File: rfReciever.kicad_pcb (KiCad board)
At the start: 2 copper layers, 82 x 40 mm, 27 parts, among them P1 USB_C_Plug_USB2.0, SW1 SW_Push, SW2 SW_Push, U1 XBee_SMT, U2 CP2102N-Axx-xQFN20, U3 USBLC6-2SC6

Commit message: Final Schematic preliminary pcb layout(pre-routing)
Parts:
- removed D3: LED, LED_SMD:LED_0603_1608Metric_Pad1.05x0.95mm_HandSolder
- removed D4: LED, LED_SMD:LED_0201_0603Metric
- removed P1: USB_C_Plug_USB2.0, Connector_USB:USB_C_Plug_JAE_DX07P024AJ1
- removed R10, R9: 10k, Resistor_SMD:R_0603_1608Metric_Pad0.98x0.95mm_HandSolder
- removed R8: 330, Resistor_SMD:R_0603_1608Metric_Pad0.98x0.95mm_HandSolder
- removed SW2: SW_Push, Button_Switch_THT:SW_PUSH_6mm_H4.3mm
- removed U2: CP2102N-Axx-xQFN20, Audio_Module:QFN24_CP2102N_SIL
- removed U3: USBLC6-2SC6, Package_TO_SOT_SMD:SOT-23-6
- added C8: 1u, Capacitor_SMD:C_0805_2012Metric, F.Cu at (93.6, 82.2)
- added D7: LED, LED_SMD:LED_0805_2012Metric, F.Cu at (77.6, 83.9)
- added D8: LED, LED_SMD:LED_0805_2012Metric, F.Cu at (122.0, 62.0)
- added D9: LED, LED_SMD:LED_0805_2012Metric, F.Cu at (118.5, 61.9)
- added P2: USB_C_Plug_USB2.0, Connector_USB:USB_C_Plug_JAE_DX07P024AJ1, F.Cu at (123.4, 71.8)
- added R11: 10K, Resistor_SMD:R_0805_2012Metric, F.Cu at (98.1, 76.9)
- added R12: 10k, Resistor_SMD:R_0805_2012Metric, F.Cu at (97.1, 83.9)
- added R15: 1K, Resistor_SMD:R_0805_2012Metric, F.Cu at (83.1, 85.9)
- added R16: 1K, Resistor_SMD:R_0805_2012Metric, F.Cu at (88.5, 61.0)
- added R17: 10k, Resistor_SMD:R_0805_2012Metric, F.Cu at (97.1, 80.9)
- added R18: 1K, Resistor_SMD:R_0805_2012Metric, F.Cu at (84.5, 61.0)
- added U4: USBLC6-2SC6, Package_TO_SOT_SMD:SOT-23-6, F.Cu at (116.0, 72.1)
- added X1: DigiXBeeRX900Micro, rfReciever-Footprints:XBeeXR900RFMicro, F.Cu at (85.1, 70.4)
- C1, C3: footprint Capacitor_SMD:C_0603_1608Metric_Pad1.08x0.95mm_HandSolder -> Capacitor_SMD:C_0805_2012Metric
- C2: footprint Capacitor_SMD:C_01005_0402Metric_Pad0.57x0.30mm_HandSolder -> Capacitor_SMD:C_0805_2012Metric
- C4: footprint Capacitor_SMD:C_0402_1005Metric_Pad0.74x0.62mm_HandSolder -> Capacitor_SMD:C_0805_2012Metric
- C5: value 1uF -> 47pF; footprint Capacitor_SMD:C_0603_1608Metric_Pad1.08x0.95mm_HandSolder -> Capacitor_SMD:C_0805_2012Metric
- C6: value 47pF -> 1uF; footprint Capacitor_SMD:C_0402_1005Metric_Pad0.74x0.62mm_HandSolder -> Capacitor_SMD:C_0805_2012Metric
- C7: footprint Capacitor_SMD:C_0805_2012Metric_Pad1.18x1.45mm_HandSolder -> Capacitor_SMD:C_0805_2012Metric
- D1: footprint LED_SMD:LED_0201_0603Metric -> LED_SMD:LED_0805_2012Metric
- D2: footprint LED_SMD:LED_0603_1608Metric_Pad1.05x0.95mm_HandSolder -> LED_SMD:LED_0805_2012Metric
- R1, R2, R3, R4: footprint Resistor_SMD:R_0603_1608Metric_Pad0.98x0.95mm_HandSolder -> Resistor_SMD:R_0805_2012Metric
- R5: value 330 -> 1K; footprint Resistor_SMD:R_0603_1608Metric_Pad0.98x0.95mm_HandSolder -> Resistor_SMD:R_0805_2012Metric
- R6: value 220 -> 1K; footprint Resistor_SMD:R_0603_1608Metric_Pad0.98x0.95mm_HandSolder -> Resistor_SMD:R_0805_2012Metric
- R7: value 220 -> 1k; footprint Resistor_SMD:R_0603_1608Metric_Pad0.98x0.95mm_HandSolder -> Resistor_SMD:R_0805_2012Metric
- SW1: value SW_Push -> RF_RESET; footprint Button_Switch_THT:SW_PUSH_6mm_H4.3mm -> Button_Switch_SMD:SW_SPST_CK_KMS2xxGP
- U1: value XBee_SMT -> CP2102N-Axx-xQFN20; footprint RF_Module:Digi_XBee_SMT -> rfReciever-Footprints:QFN50P500X500X80-29N
- moved C7 38.6 mm to (77.6, 80.6), turned to 180 degrees
- moved C6 36.9 mm to (81.1, 82.6), turned to -90 degrees
- moved SW1 30.4 mm to (89.1, 82.2)
- moved C1 30.2 mm to (104.8, 77.6)
- moved R5 29.5 mm to (112.0, 65.9), turned to 90 degrees
- moved U1 27.7 mm to (105.9, 72.6), turned to 0 degrees
- moved R7 27.7 mm to (95.1, 86.4)
- moved R1 26.0 mm to (106.0, 64.9)
- moved C2 24.8 mm to (100.6, 71.9), turned to 90 degrees
- moved R4 24.5 mm to (111.1, 77.7), turned to 180 degrees
- moved C5 23.9 mm to (84.1, 82.6), turned to -90 degrees
- moved C4 19.9 mm to (101.8, 68.1), turned to 0 degrees
- moved D1 18.7 mm to (112.0, 61.9), turned to -90 degrees
- moved C3 17.1 mm to (101.8, 65.1), turned to 0 degrees
- moved R6 9.47 mm to (115.0, 66.0), turned to 90 degrees
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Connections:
- net Net-(D1-A) renamed /BRIDGE_D1
- net Net-(D2-A) renamed /BRIDGE_D2
- C1 pad 1: /5V(in) -> +5V
- C2 pad 1: /5V(in) -> +5V
- C3 pad 2: /3.3V (out) -> +3.3V
- C4 pad 2: /3.3V (out) -> +3.3V
- C5 pad 1: /3.3V (out) -> +3.3V
- C6 pad 1: /3.3V (out) -> +3.3V
- C7 pad 1: /3.3V (out) -> +3.3V
- R1 pad 1: /3.3V (out) -> /BRIDGE_3.3
- R1 pad 2: Net-(U2-~{RST}) -> +3.3V
- R2 pad 1: Net-(U2-VBUS) -> /BRIDGE_VBUS
- R3 pad 1: /5V(in) -> +5V
- R3 pad 2: Net-(U2-VBUS) -> /BRIDGE_VBUS
- R5 pad 1: Net-(U1-DIO5/ASSOCIATE) -> /TXD(Bridge)
- R6 pad 1: Net-(U1-DIO13/UART_TX) -> /RXD(Bridge)
- R7 pad 1: Net-(U1-DIO14/UART_RX/~{CONFIG}) -> /RF_RESET
- R7 pad 2: Net-(D3-A) -> /RF_RESET
- SW1 pad 1: GND -> /RF_RESET
- SW1 pad 2: Net-(U1-RESET/OD_OUT) -> GND
- U1 pad 1: GND -> unconnected-(U1-RS485/GPIO.1-Pad1)
- U1 pad 10: Net-(U1-DIO8/SLEEP_REQUEST) -> unconnected-(U1-NC-Pad10)
- U1 pad 11: GND -> unconnected-(U1-~{SUSPEND}-Pad11)
- U1 pad 12: unconnected-(U1-DIO19/SPI_~{ATTN}-Pad12) -> GND
- U1 pad 13: GND -> unconnected-(U1-~{WAKEUP}-Pad13)
- U1 pad 15: unconnected-(U1-DIO17/SPI_~{SSEL}-Pad15) -> /CTS(Bridge)
- U1 pad 16: unconnected-(U1-DIO16/SPI_MOSI-Pad16) -> /RTS(Bridge)
- U1 pad 17: unconnected-(U1-DIO15/SPI_MISO-Pad17) -> /RXD(Bridge)
- U1 pad 18: unconnected-(U1-NC-Pad18) -> /TXD(Bridge)
- U1 pad 2: /3.3V (out) -> unconnected-(U1-CLK/GPIO.0-Pad2)
- U1 pad 21: unconnected-(U1-NC-Pad21) -> GND
- U1 pad 22: GND -> (no net)
- U1 pad 23: unconnected-(U1-NC-Pad23) -> (no net)
- U1 pad 24: unconnected-(U1-DIO4-Pad24) -> (no net)
- U1 pad 25: Net-(U1-DIO7/~{CTS}) -> (no net)
- U1 pad 26: unconnected-(U1-DIO9/ON/~{SLEEP}-Pad26) -> (no net)
- U1 pad 27: unconnected-(U1-VREF-Pad27) -> (no net)
- U1 pad 28: Net-(U1-DIO5/ASSOCIATE) -> (no net)
- U1 pad 29: Net-(U1-DIO6/~{RTS}) -> (no net)
- U1 pad 3: Net-(U1-DIO13/UART_TX) -> GND
- U1 pad 4: Net-(U1-DIO14/UART_RX/~{CONFIG}) -> /USB_D+
- U1 pad 5: unconnected-(U1-DIO12-Pad5) -> /USB_D-
- U1 pad 6: Net-(U1-RESET/OD_OUT) -> +3.3V
- U1 pad 7: Net-(U1-DIO10/RSSI/PWM0) -> +5V
- U1 pad 8: unconnected-(U1-DIO11/PWM1-Pad8) -> /BRIDGE_VBUS
- U1 pad 9: unconnected-(U1-NC-Pad9) -> /BRIDGE_3.3
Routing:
- net /3.3V (out): track 87.0 -> 0.00 mm, vias 2 -> 0
- net Net-(U1-DIO13/UART_TX): track 74.9 -> 0.00 mm, vias 4 -> 0
- net /5V(in): track 67.7 -> 0.00 mm, vias 2 -> 0
- net Net-(U1-DIO14/UART_RX/~{CONFIG}): track 66.0 -> 0.00 mm, vias 2 -> 0
- net Net-(U1-RESET/OD_OUT): track 55.3 -> 0.00 mm
- net Net-(U1-DIO6/~{RTS}): track 48.0 -> 0.00 mm, vias 2 -> 0
- net Net-(U1-DIO7/~{CTS}): track 47.5 -> 0.00 mm
- net GND: track 42.2 -> 0.00 mm, vias 23 -> 0
- net Net-(U1-DIO8/SLEEP_REQUEST): track 25.0 -> 0.00 mm
- net Net-(D4-A): track 22.7 -> 0.00 mm
- net Net-(U2-D-): track 21.2 -> 0.00 mm, vias 2 -> 0
- net /D-: track 13.0 -> 0.00 mm
- net /D+: track 11.6 -> 0.00 mm
- net /BRIDGE_D1: track 11.3 -> 0.00 mm
- net Net-(U2-~{RST}): track 10.3 -> 0.00 mm, vias 2 -> 0
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- removed copper zone on B.Cu, net GND
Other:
- board size 82 x 40 mm -> 5 x 8.2 mm
- board text removed: "U2"

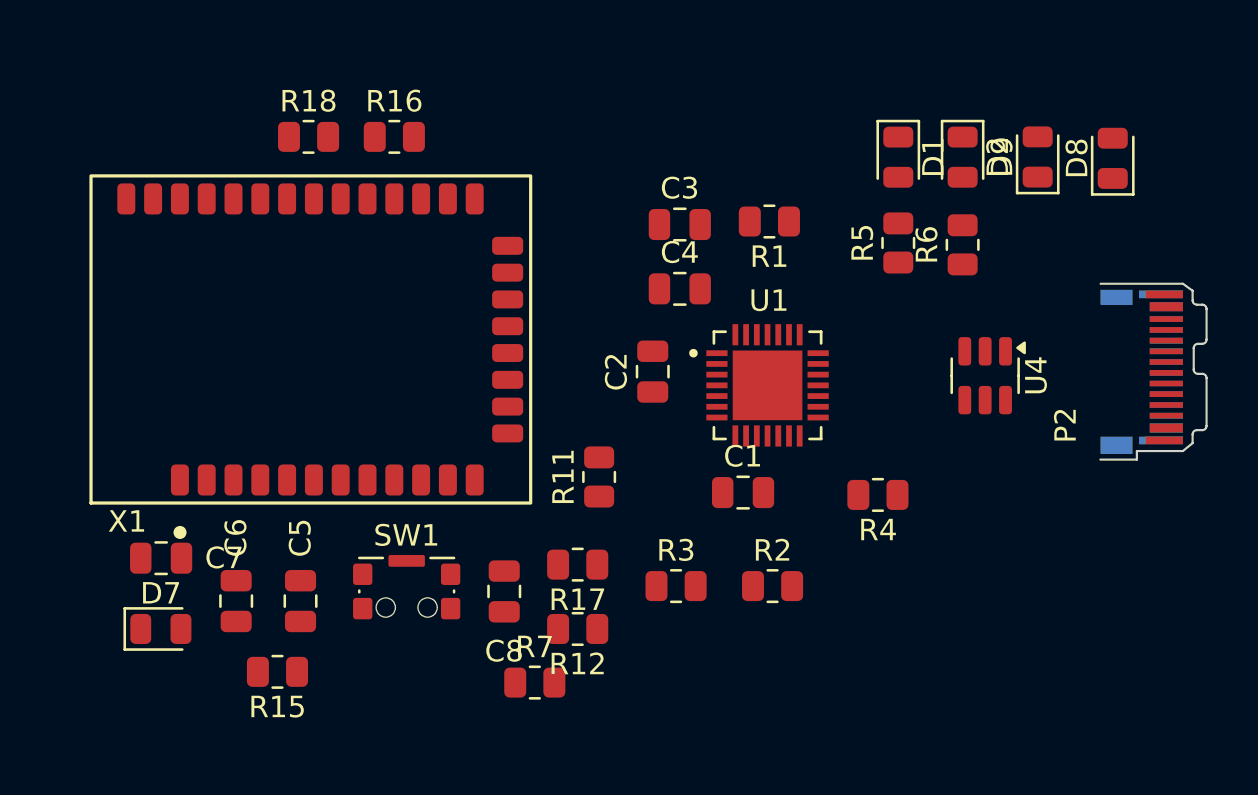
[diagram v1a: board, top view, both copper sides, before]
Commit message: Routing V1, possibly not DRC compliant
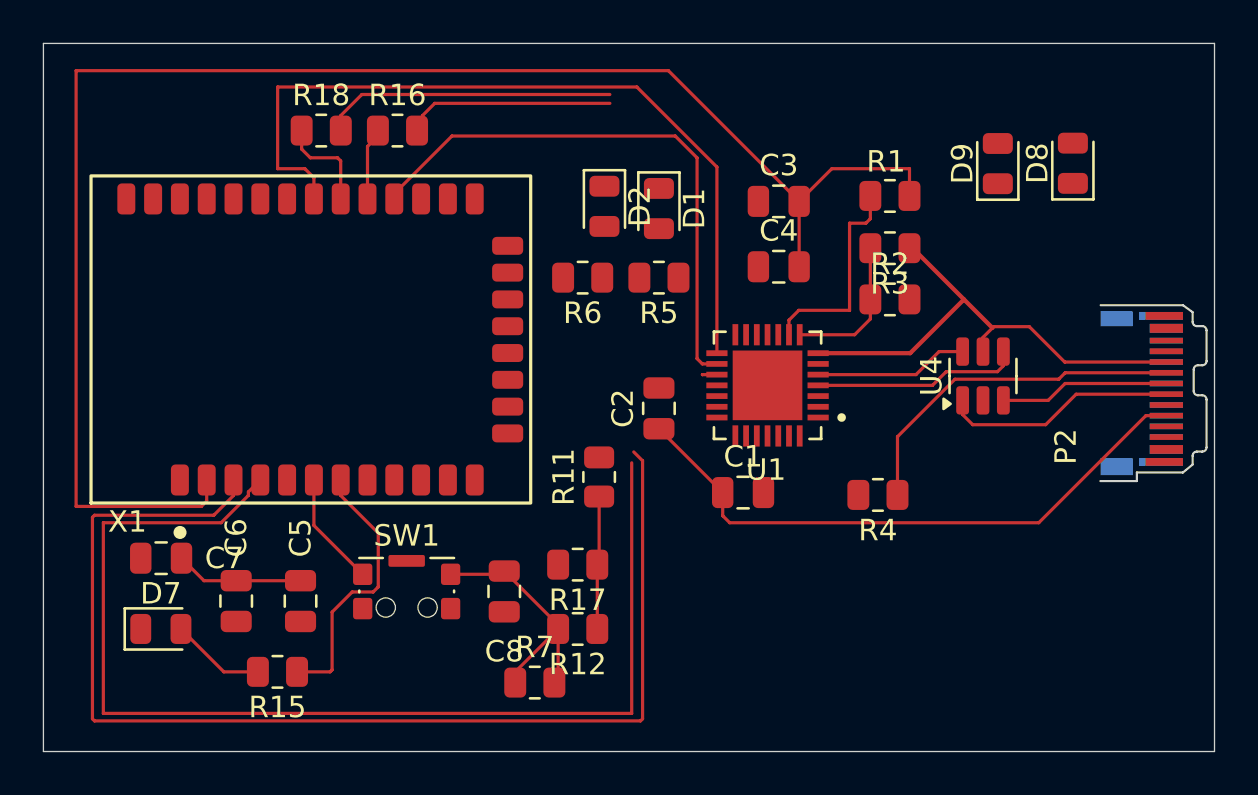
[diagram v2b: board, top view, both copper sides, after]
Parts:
- moved R3 18.6 mm to (111.6, 66.2), turned to 180 degrees
- moved R6 17.8 mm to (97.3, 67.6), turned to 180 degrees
- moved D2 16.9 mm to (98.3, 64.2)
- moved R2 14.4 mm to (111.6, 68.6)
- moved D1 11.4 mm to (100.8, 64.3)
- moved R5 11.3 mm to (100.8, 67.6), turned to 180 degrees
- moved R1 5.74 mm to (111.6, 63.8), turned to 0 degrees
- moved C3 4.74 mm to (106.4, 64.0)
- moved C4 4.73 mm to (106.4, 67.1)
- moved D9 1.88 mm to (116.6, 62.2)
- moved D8 1.87 mm to (120.1, 62.2)
- moved C2 1.74 mm to (100.8, 73.7)
- moved P2 1.00 mm to (123.4, 72.8)
- moved R18 0.66 mm to (85.1, 60.7)
- moved R16 0.33 mm to (88.6, 60.7)
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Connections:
- U1 pad 4: /USB_D+ -> /USB_OUT_D+
- U1 pad 5: /USB_D- -> /USB_OUT_D-
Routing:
- net +3.3V: track 0.00 -> 86.0 mm
- net /RXD(Bridge): track 0.00 -> 56.2 mm
- net /TXD(Bridge): track 0.00 -> 53.5 mm
- net +5V: track 0.00 -> 51.5 mm
- net /CTS(Bridge): track 0.00 -> 37.4 mm
- net /RTS(Bridge): track 0.00 -> 26.3 mm
- net /RF_RESET: track 0.00 -> 17.5 mm
- net Net-(P2-CC): track 0.00 -> 16.5 mm
- net /RF_D9: track 0.00 -> 13.7 mm
- net /RF_PWM: track 0.00 -> 12.7 mm
- net /USB_IN_D-: track 0.00 -> 10.9 mm
- net /BRIDGE_3.3: track 0.00 -> 9.88 mm
- net /USB_OUT_D+: track 0.00 -> 9.68 mm
- net /RF_D8: track 0.00 -> 9.68 mm
- net /USB_IN_D+: track 0.00 -> 7.93 mm
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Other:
- board size 5 x 8.2 mm -> 54.6 x 33 mm

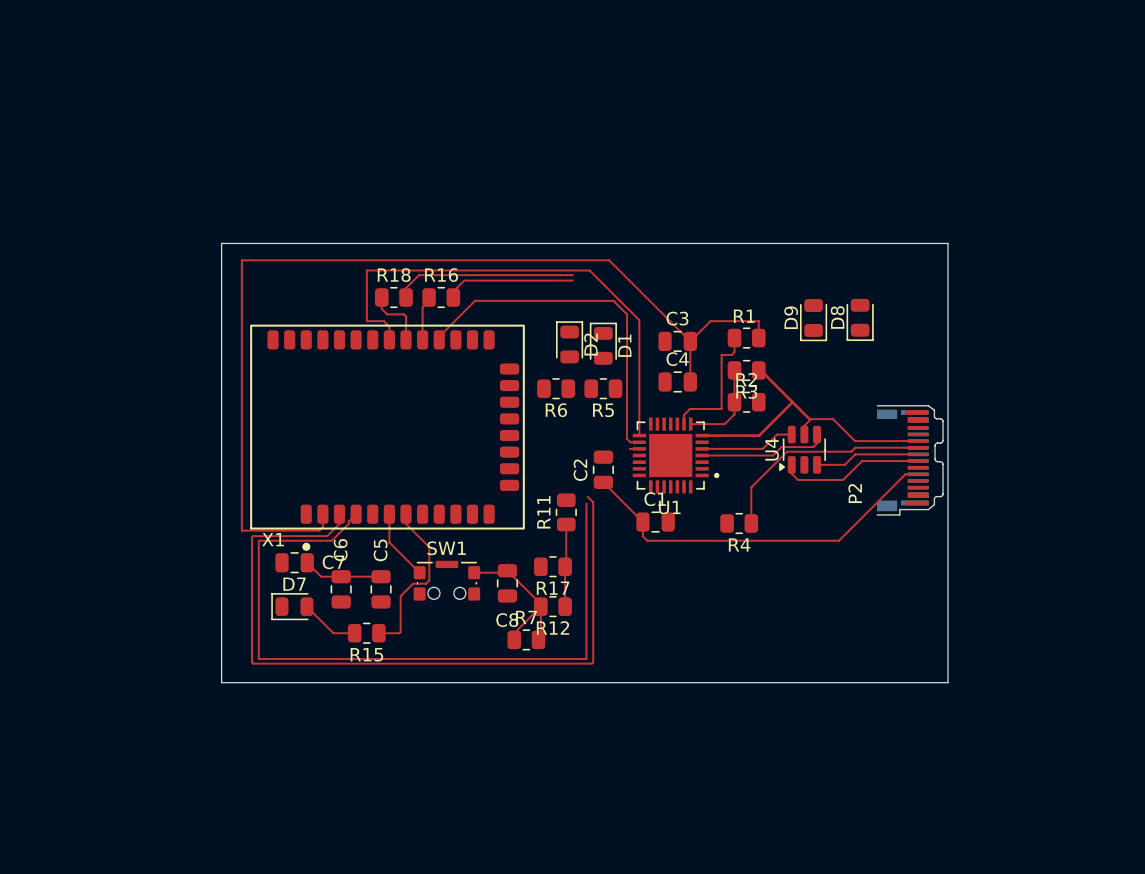
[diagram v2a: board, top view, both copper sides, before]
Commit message: Reworked schematic, partial layout
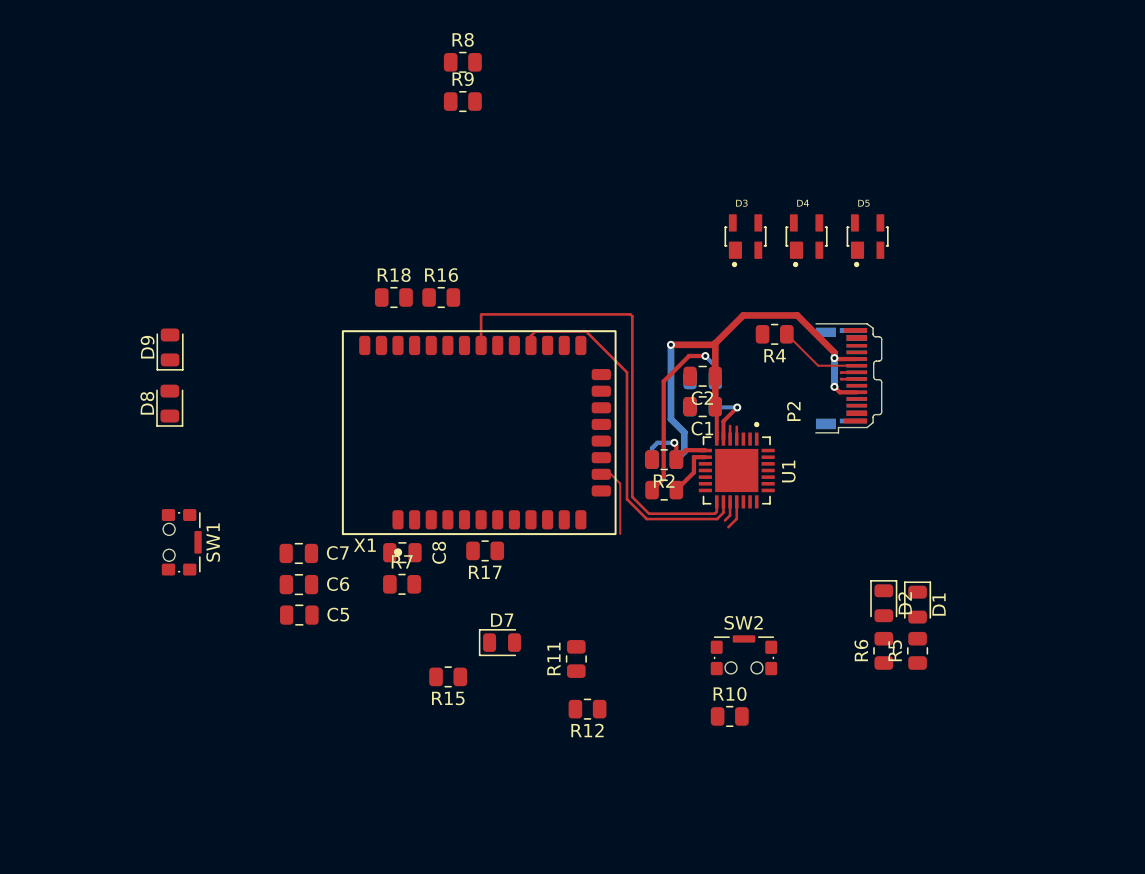
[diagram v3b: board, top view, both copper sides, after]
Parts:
- removed U4: USBLC6-2SC6, Package_TO_SOT_SMD:SOT-23-6
- added D3: SP0503BAHTG, rfReciever-Footprints:SOT143, F.Cu at (111.5, 56.1)
- added D4: SP0503BAHTG, rfReciever-Footprints:SOT143, F.Cu at (116.1, 56.1)
- added D5: SP0503BAHTG, rfReciever-Footprints:SOT143, F.Cu at (120.7, 56.1)
- added R10: 10k, Resistor_SMD:R_0805_2012Metric, F.Cu at (110.3, 92.2)
- added R8: 10K, Resistor_SMD:R_0805_2012Metric, F.Cu at (90.3, 43.0)
- added R9: 10K, Resistor_SMD:R_0805_2012Metric, F.Cu at (90.3, 46.0)
- added SW2: RF_RESET, Button_Switch_SMD:SW_SPST_CK_KMS2xxGP, F.Cu at (111.4, 87.8)
- C3, C4, R3: moved to B.Cu
- C6: value 1uF -> 1F
- C7: value 10uF -> 10F
- moved D8 52.3 mm to (68.2, 68.7)
- moved D9 48.4 mm to (68.3, 64.5)
- moved R6 31.6 mm to (121.9, 87.3), turned to 90 degrees
- moved R5 30.8 mm to (124.5, 87.3), turned to 90 degrees
- moved D1 30.6 mm to (124.5, 83.8)
- moved D2 30.6 mm to (121.9, 83.7)
- moved SW1 20.4 mm to (68.9, 79.1), turned to -90 degrees
- moved D7 15.8 mm to (93.2, 86.7)
- moved R4 14.5 mm to (113.7, 63.5)
- moved R1 13.0 mm to (105.4, 75.2), turned to 180 degrees
- moved R11 11.1 mm to (98.8, 87.9)
- moved C2 10.3 mm to (108.3, 66.6), turned to 180 degrees
- moved R7 10.2 mm to (85.7, 82.3)
- moved C1 9.37 mm to (108.3, 68.9), turned to 180 degrees
- moved R3 9.13 mm to (105.4, 72.9)
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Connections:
- net /CTS(Bridge) renamed /UART_CTS
- net /RTS(Bridge) renamed /UART_RTS
- P2 pad A4: +5V -> Net-(D3-Pad1)
- P2 pad A9: +5V -> Net-(D3-Pad1)
- P2 pad B4: +5V -> Net-(D3-Pad1)
- P2 pad B9: +5V -> Net-(D3-Pad1)
- R5 pad 1: /TXD(Bridge) -> Net-(U1-~{TXT}/GPIO.2)
- R6 pad 1: /RXD(Bridge) -> Net-(U1-~{RXT}/GPIO.3)
- R7 pad 2: /RF_RESET -> /RF_SW_RSTO
- SW1 pad 1: /RF_RESET -> /RF_SW_RSTO
- U1 pad 17: /RXD(Bridge) -> /RF_RXD
- U1 pad 18: /TXD(Bridge) -> /RF_TXD
- U1 pad 19: unconnected-(U1-~{RXT}/GPIO.3-Pad19) -> Net-(U1-~{RXT}/GPIO.3)
- U1 pad 20: unconnected-(U1-~{TXT}/GPIO.2-Pad20) -> Net-(U1-~{TXT}/GPIO.2)
- X1 pad 3: /RXD(Bridge) -> /RF_RXD
- X1 pad 4: /TXD(Bridge) -> /RF_TXD
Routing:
- net +3.3V: track 86.0 -> 21.1 mm, vias 0 -> 2
- net /RXD(Bridge): track 56.2 -> 0.00 mm
- net /TXD(Bridge): track 53.5 -> 0.00 mm
- net /RF_RESET: track 17.5 -> 0.00 mm
- net +5V: track 51.5 -> 37.0 mm, vias 0 -> 3
- net /RF_D9: track 13.7 -> 0.00 mm
- net /RF_PWM: track 12.7 -> 0.00 mm
- net Net-(P2-CC): track 16.5 -> 6.23 mm
- net /USB_IN_D-: track 10.9 -> 1.20 mm
- net /RF_D8: track 9.68 -> 0.00 mm
- net /USB_OUT_D+: track 9.68 -> 0.92 mm
- net /USB_IN_D+: track 7.93 -> 1.20 mm
- net /USB_OUT_D-: track 7.18 -> 0.99 mm
- net /BRIDGE_3.3: track 9.88 -> 3.97 mm
- net Net-(X1-SPI_N_SSEL/DIO17): track 0.00 -> 5.50 mm
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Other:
- board size 54.6 x 33 mm -> 5 x 8.2 mm

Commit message: layout+routing v2, TODO: rework USB routing
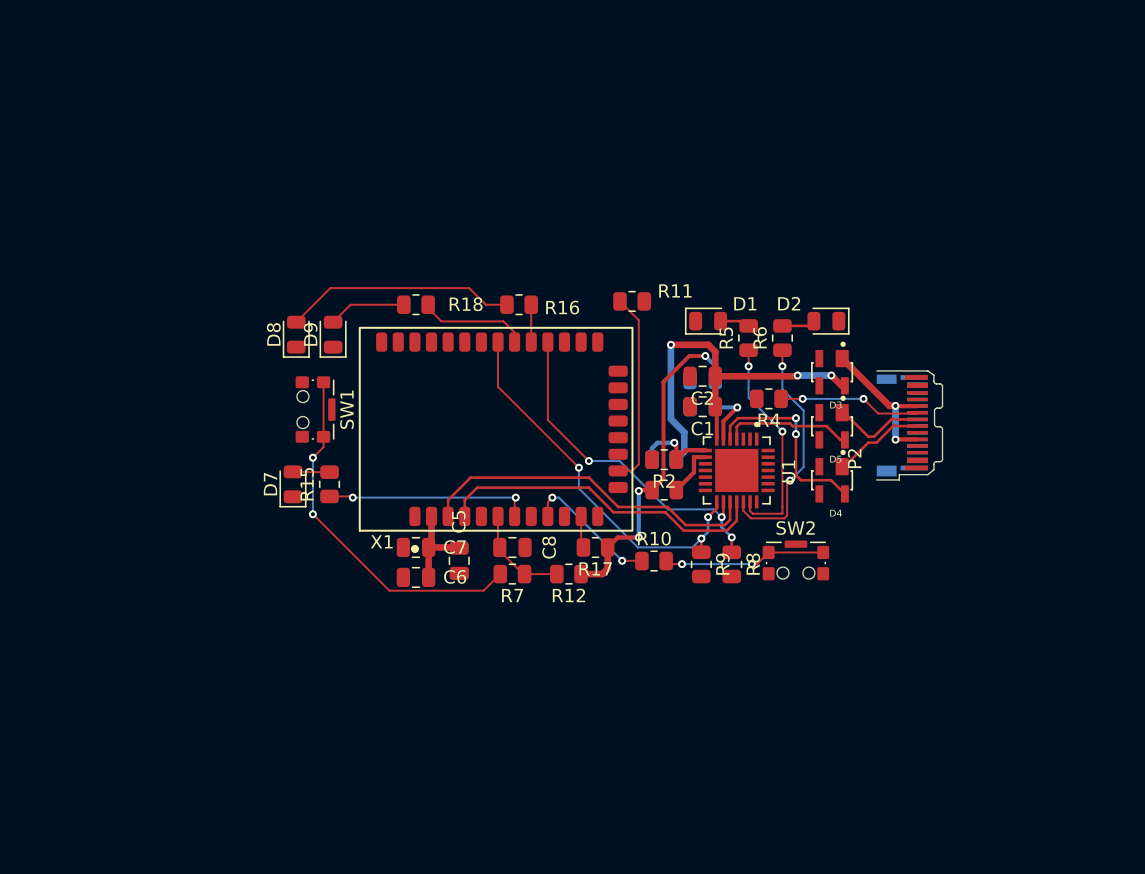
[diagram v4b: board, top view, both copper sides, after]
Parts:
- moved R8 42.8 mm to (110.5, 80.8), turned to -90 degrees
- moved R9 39.1 mm to (108.2, 80.8), turned to -90 degrees
- moved R11 27.2 mm to (103.0, 61.0), turned to 180 degrees
- moved R5 26.7 mm to (111.8, 63.8)
- moved D1 26.5 mm to (108.7, 62.5), turned to 0 degrees
- moved R6 24.7 mm to (114.3, 63.8)
- moved D2 21.6 mm to (117.6, 62.5), turned to 180 degrees
- moved D7 19.7 mm to (77.5, 74.8), turned to 90 degrees
- moved D4 18.4 mm to (118.0, 74.5), turned to 180 degrees
- moved R15 17.0 mm to (80.2, 74.8), turned to 90 degrees
- moved D5 14.5 mm to (118.0, 70.4), turned to 180 degrees
- moved SW1 14.2 mm to (79.0, 69.1)
- moved R10 13.0 mm to (104.6, 80.5)
- moved C5 12.7 mm to (90.0, 80.5), turned to -90 degrees
- moved D9 12.3 mm to (80.5, 63.5)
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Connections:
- R16 pad 1: /RF_SLEEP -> /RF_DSLEEP
- X1 pad 25: /RF_SLEEP -> /RF_DSLEEP
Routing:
- net /RF_SW_RSTO: track 0.00 -> 27.2 mm, vias 0 -> 2
- net /RF_RXD: track 1.56 -> 26.1 mm
- net /RF_TXD: track 2.17 -> 25.1 mm
- net +3.3V: track 21.1 -> 39.0 mm, vias 2 -> 4
- net Net-(U1-~{RXT}/GPIO.3): track 0.00 -> 17.9 mm, vias 0 -> 2
- net /RF_D8: track 0.00 -> 17.4 mm
- net Net-(U1-~{TXT}/GPIO.2): track 0.00 -> 16.5 mm, vias 0 -> 2
- net /RF_PWM: track 0.00 -> 15.5 mm, vias 0 -> 2
- net /USB_OUT_D-: track 0.99 -> 14.7 mm, vias 0 -> 2
- net Net-(R10-Pad2): track 0.00 -> 12.3 mm, vias 0 -> 2
- net Net-(D3-Pad1): track 0.00 -> 11.4 mm, vias 0 -> 2
- net /RF_SLEEP: track 0.00 -> 10.3 mm, vias 0 -> 2
- net Net-(X1-SPI_N_SSEL/DIO17): track 5.50 -> 14.6 mm
- net /USB_OUT_D+: track 0.92 -> 9.67 mm
- net /RF_RESET: track 0.00 -> 8.09 mm
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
